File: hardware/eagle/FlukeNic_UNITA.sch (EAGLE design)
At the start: 29 parts, among them CN1 PS-10PE-D4T2-M1E, CN2 B-057-HP, CN3 B-057-HP, U1 NJM7805SDL1, U2 NJM2845DL1-33, U3 UNITB, U4 LM339N

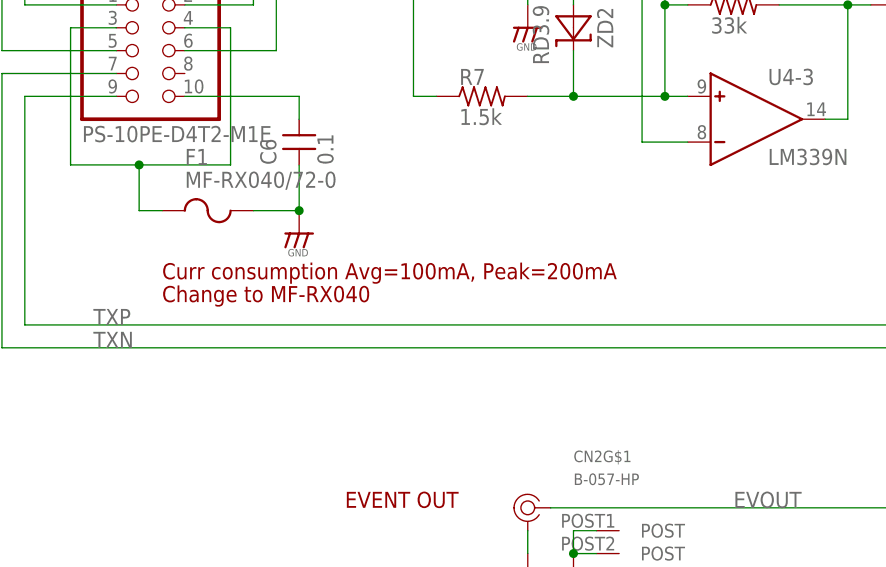
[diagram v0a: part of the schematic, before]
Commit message: Fuse F1 not used, use jumper instead.
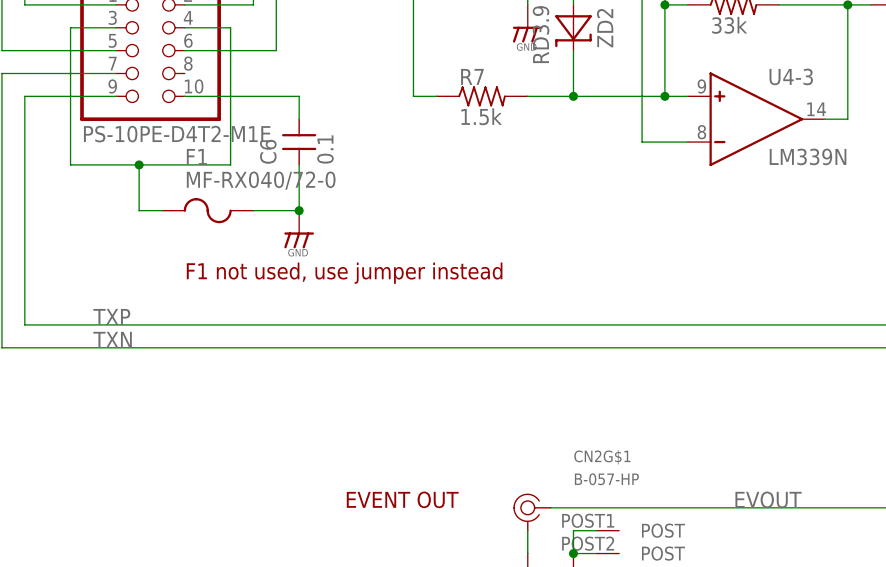
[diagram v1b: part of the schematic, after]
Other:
- note added: "F1 not used, use jumper instead"
- note removed: "Change to MF-RX040"
- note removed: "Curr consumption Avg=100mA, Peak=200mA"
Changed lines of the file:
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@@
 <grid distance="0.1" unitdist="inch" unit="inch" style="lines" multiple="1" display="no" altdistance="0.01" altunitdist="inch" altunit="inch"/>
 <layers>
-<layer number="1" name="Top" color="4" fill="1" visible="yes" active="no"/>
-<layer number="2" name="Route2" color="1" fill="3" visible="yes" active="no"/>
-<layer number="3" name="Route3" color="4" fill="3" visible="yes" active="no"/>
-<layer number="4" name="Route4" color="1" fill="4" visible="yes" active="no"/>
-<layer number="5" name="Route5" color="4" fill="4" visible="yes" active="no"/>
-<layer number="6" name="Route6" color="1" fill="8" visible="yes" active="no"/>
-<layer number="7" name="Route7" color="4" fill="8" visible="yes" active="no"/>
-<layer number="8" name="Route8" color="1" fill="2" visible="yes" active="no"/>
-<layer number="9" name="Route9" color="4" fill="2" visible="yes" active="no"/>
-<layer number="10" name="Route10" color="1" fill="7" visible="yes" active="no"/>
-<layer number="11" name="Route11" color="4" fill="7" visible="yes" active="no"/>
-<layer number="12" name="Route12" color="1" fill="5" visible="yes" active="no"/>
-<layer number="13" name="Route13" color="4" fill="5" visible="yes" active="no"/>
-<layer number="14" name="Route14" color="1" fill="6" visible="yes" active="no"/>
-<layer number="15" name="Route15" color="4" fill="6" visible="yes" active="no"/>
-<layer number="16" name="Bottom" color="1" fill="1" visible="yes" active="no"/>
-<layer number="17" name="Pads" color="2" fill="1" visible="yes" active="no"/>
-<layer number="18" name="Vias" color="2" fill="1" visible="yes" active="no"/>
-<layer number="19" name="Unrouted" color="6" fill="1" visible="yes" active="no"/>
-<layer number="20" name="Dimension" color="15" fill="1" visible="yes" active="no"/>
-<layer number="21" name="tPlace" color="7" fill="1" visible="yes" active="no"/>
-<layer number="22" name="bPlace" color="7" fill="1" visible="yes" active="no"/>
-<layer number="23" name="tOrigins" color="15" fill="1" visible="yes" active="no"/>
-<layer number="24" name="bOrigins" color="15" fill="1" visible="yes" active="no"/>
-<layer number="25" name="tNames" color="7" fill="1" visible="yes" active="no"/>
-<layer number="26" name="bNames" color="7" fill="1" visible="yes" active="no"/>
-<layer number="27" name="tValues" color="7" fill="1" visible="yes" active="no"/>
-<layer number="28" name="bValues" color="7" fill="1" visible="yes" active="no"/>
+<layer number="1" name="Top" color="4" fill="1" visible="no" active="no"/>
+<layer number="2" name="Route2" color="1" fill="3" visible="no" active="no"/>
+<layer number="3" name="Route3" color="4" fill="3" visible="no" active="no"/>
+<layer number="4" name="Route4" color="1" fill="4" visible="no" active="no"/>
+<layer number="5" name="Route5" color="4" fill="4" visible="no" active="no"/>
+<layer number="6" name="Route6" color="1" fill="8" visible="no" active="no"/>
+<layer number="7" name="Route7" color="4" fill="8" visible="no" active="no"/>
+<layer number="8" name="Route8" color="1" fill="2" visible="no" active="no"/>
+<layer number="9" name="Route9" color="4" fill="2" visible="no" active="no"/>
+<layer number="10" name="Route10" color="1" fill="7" visible="no" active="no"/>
+<layer number="11" name="Route11" color="4" fill="7" visible="no" active="no"/>
+<layer number="12" name="Route12" color="1" fill="5" visible="no" active="no"/>
+<layer number="13" name="Route13" color="4" fill="5" visible="no" active="no"/>
+<layer number="14" name="Route14" color="1" fill="6" visible="no" active="no"/>
+<layer number="15" name="Route15" color="4" fill="6" visible="no" active="no"/>
+<layer number="16" name="Bottom" color="1" fill="1" visible="no" active="no"/>
+<layer number="17" name="Pads" color="2" fill="1" visible="no" active="no"/>
+<layer number="18" name="Vias" color="2" fill="1" visible="no" active="no"/>
+<layer number="19" name="Unrouted" color="6" fill="1" visible="no" active="no"/>
+<layer number="20" name="Dimension" color="15" fill="1" visible="no" active="no"/>
+<layer number="21" name="tPlace" color="7" fill="1" visible="no" active="no"/>
+<layer number="22" name="bPlace" color="7" fill="1" visible="no" active="no"/>
+<layer number="23" name="tOrigins" color="15" fill="1" visible="no" active="no"/>
+<layer number="24" name="bOrigins" color="15" fill="1" visible="no" active="no"/>
+<layer number="25" name="tNames" color="7" fill="1" visible="no" active="no"/>
+<layer number="26" name="bNames" color="7" fill="1" visible="no" active="no"/>
+<layer number="27" name="tValues" color="7" fill="1" visible="no" active="no"/>
+<layer number="28" name="bValues" color="7" fill="1" visible="no" active="no"/>
 <layer number="29" name="tStop" color="7" fill="3" visible="no" active="no"/>
 <layer number="30" name="bStop" color="7" fill="6" visible="no" active="no"/>
@@
 <layer number="35" name="tGlue" color="7" fill="4" visible="no" active="no"/>
 <layer number="36" name="bGlue" color="7" fill="5" visible="no" active="no"/>
-<layer number="37" name="tTest" color="7" fill="1" visible="yes" active="no"/>
-<layer number="38" name="bTest" color="7" fill="1" visible="yes" active="no"/>
+<layer number="37" name="tTest" color="7" fill="1" visible="no" active="no"/>
+<layer number="38" name="bTest" color="7" fill="1" visible="no" active="no"/>
 <layer number="39" name="tKeepout" color="4" fill="11" visible="no" active="no"/>
 <layer number="40" name="bKeepout" color="1" fill="11" visible="no" active="no"/>
@@
 <layer number="44" name="Drills" color="7" fill="1" visible="no" active="no"/>
 <layer number="45" name="Holes" color="7" fill="1" visible="no" active="no"/>
-<layer number="46" name="Milling" color="3" fill="1" visible="yes" active="no"/>
-<layer number="47" name="Measures" color="7" fill="1" visible="yes" active="no"/>
-<layer number="48" name="Document" color="7" fill="1" visible="yes" active="no"/>
-<layer number="49" name="Reference" color="7" fill="1" visible="yes" active="no"/>
-<layer number="50" name="dxf" color="7" fill="1" visible="yes" active="no"/>
-<layer number="51" name="tDocu" color="7" fill="1" visible="yes" active="no"/>
-<layer number="52" name="bDocu" color="7" fill="1" visible="yes" active="no"/>
+<layer number="46" name="Milling" color="3" fill="1" visible="no" active="no"/>
+<layer number="47" name="Measures" color="7" fill="1" visible="no" active="no"/>
+<layer number="48" name="Document" color="7" fill="1" visible="no" active="no"/>
+<layer number="49" name="Reference" color="7" fill="1" visible="no" active="no"/>
+<layer number="50" name="dxf" color="7" fill="1" visible="no" active="no"/>
+<layer number="51" name="tDocu" color="7" fill="1" visible="no" active="no"/>
+<layer number="52" name="bDocu" color="7" fill="1" visible="no" active="no"/>
 <layer number="88" name="SimResults" color="9" fill="1" visible="yes" active="yes"/>
 <layer number="89" name="SimProbes" color="9" fill="1" visible="yes" active="yes"/>
@@
 <text x="53.34" y="38.1" size="1.778" layer="94">EVENT IN</text>
 <text x="66.04" y="205.74" size="1.778" layer="94">10V approx</text>
-<text x="33.02" y="81.28" size="1.778" layer="94">Curr consumption Avg=100mA, Peak=200mA</text>
-<text x="33.02" y="78.74" size="1.778" layer="94">Change to MF-RX040</text>
+<text x="35.56" y="81.28" size="1.778" layer="94">F1 not used, use jumper instead</text>
 </plain>
 <instances>
